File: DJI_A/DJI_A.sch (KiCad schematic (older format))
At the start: 3 parts, among them J1 Conn_01x26, J2 Conn_01x26, J3 Conn_02x13_Odd_Even

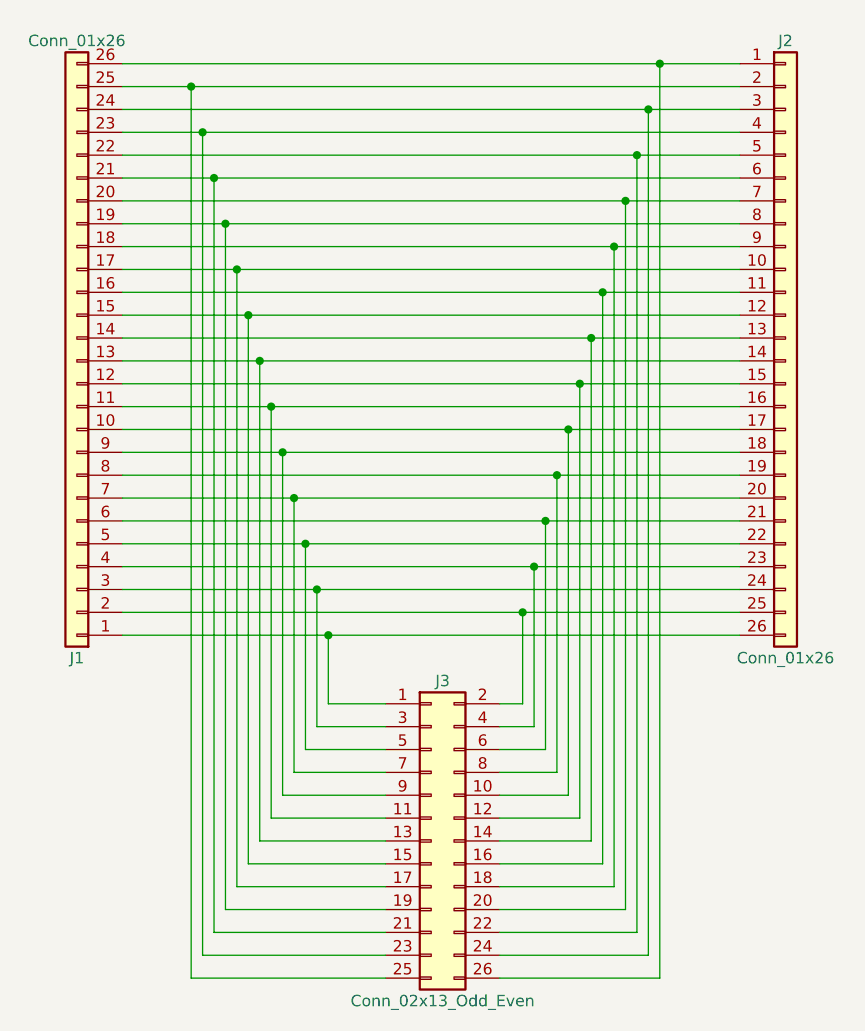
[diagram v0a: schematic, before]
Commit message: Possible straight-through pinout. Don't use this version.
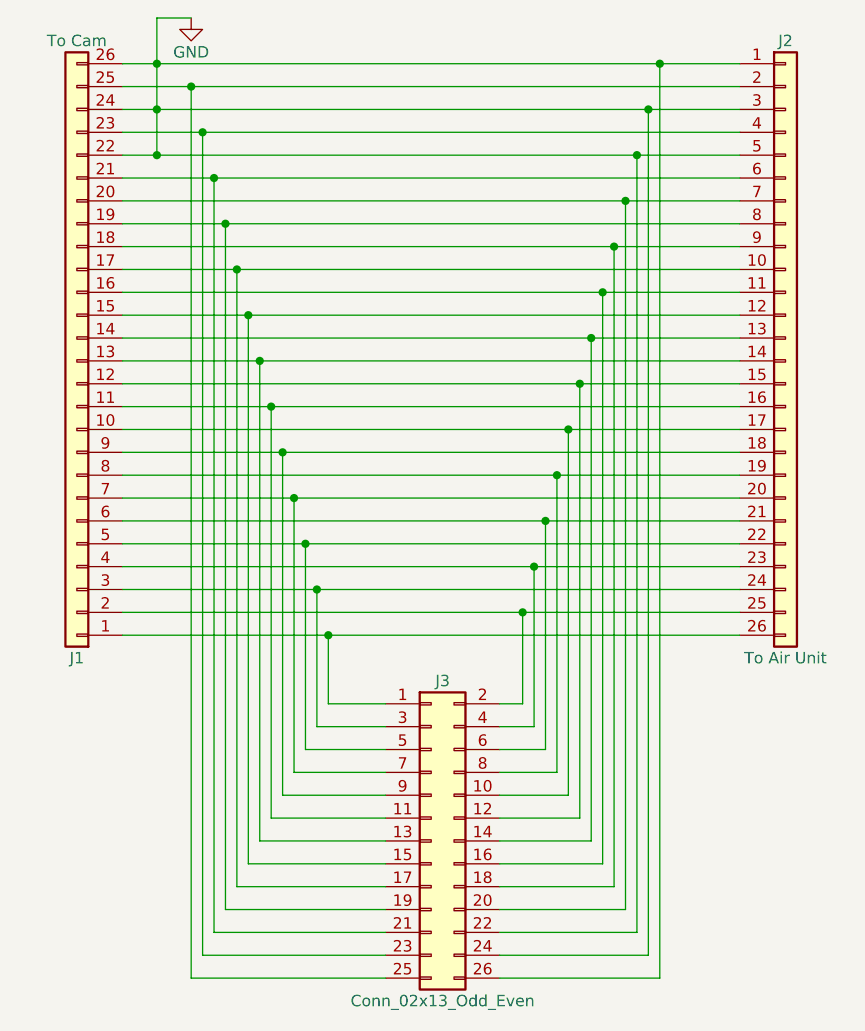
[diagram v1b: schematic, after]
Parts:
- J1: value Conn_01x26 -> To Cam; footprint (none) -> UserLib:DF56C-26S
- J2: value Conn_01x26 -> To Air Unit; footprint (none) -> UserLib:DF56C-26S
- J3: footprint (none) -> Connector_PinHeader_2.54mm:PinHeader_2x13_P2.54mm_Vertical
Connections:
- net GND: now reaches J1.26 (Pin_26), J2.1 (Pin_1), J3.26 (Pin_26)
- net GND: now also J1.22 (Pin_22), J1.24 (Pin_24), J2.3 (Pin_3), J2.5 (Pin_5), J3.22 (Pin_22), J3.24 (Pin_24)
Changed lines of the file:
@@
 P 4200 2050
 F 0 "J2" H 4200 3350 50  0000 C CNN
-F 1 "Conn_01x26" H 4200 650 50  0000 C CNN
-F 2 "" H 4200 2050 50  0001 C CNN
+F 1 "To Air Unit" H 4200 650 50  0000 C CNN
+F 2 "UserLib:DF56C-26S" H 4200 2050 50  0001 C CNN
 F 3 "~" H 4200 2050 50  0001 C CNN
 	1    4200 2050
@@
 P 1100 2150
 F 0 "J1" H 1100 3450 50  0000 C CNN
-F 1 "Conn_01x26" H 1100 750 50  0000 C CNN
-F 2 "" H 1100 2150 50  0001 C CNN
+F 1 "To Cam" H 1100 750 50  0000 C CNN
+F 2 "UserLib:DF56C-26S" H 1100 2150 50  0001 C CNN
 F 3 "~" H 1100 2150 50  0001 C CNN
 	1    1100 2150
@@
 $EndComp
 Wire Wire Line
-	1300 850  3650 850
-Wire Wire Line
-	1300 950  1600 950
-Wire Wire Line
-	1300 1050 3600 1050
-Wire Wire Line
 	1300 1150 1650 1150
 Wire Wire Line
-	1300 1250 3550 1250
+	1300 1250 1450 1250
 Wire Wire Line
 	1300 1350 1700 1350
@@
 F 0 "J3" H 2700 4950 50  0000 C CNN
 F 1 "Conn_02x13_Odd_Even" H 2700 3550 50  0000 C CNN
-F 2 "" H 2650 4250 50  0001 C CNN
+F 2 "Connector_PinHeader_2.54mm:PinHeader_2x13_P2.54mm_Vertical" H 2650 4250 50  0001 C CNN
 F 3 "~" H 2650 4250 50  0001 C CNN
 	1    2650 4250
@@
 Wire Wire Line
 	3650 850  4000 850
+Wire Wire Line
+	1300 1050 1450 1050
+Wire Wire Line
+	1300 950  1600 950
+Wire Wire Line
+	1300 850  1450 850
+Wire Wire Line
+	1450 850  1450 1050
+Connection ~ 1450 850
+Wire Wire Line
+	1450 850  3650 850
+Connection ~ 1450 1050
+Wire Wire Line
+	1450 1050 3600 1050
+Wire Wire Line
+	1450 1050 1450 1250
+Connection ~ 1450 1250
+Wire Wire Line
+	1450 1250 3550 1250
+$Comp
+L power:GND #PWR?
+U 1 1 61E21795
+P 1600 650
+F 0 "#PWR?" H 1600 400 50  0001 C CNN
+F 1 "GND" H 1600 500 50  0000 C CNN
+F 2 "" H 1600 650 50  0001 C CNN
+F 3 "" H 1600 650 50  0001 C CNN
+	1    1600 650
+	1    0    0    -1
+$EndComp
+Wire Wire Line
+	1450 850  1450 650
+Wire Wire Line
+	1450 650  1600 650
 $EndSCHEMATC
